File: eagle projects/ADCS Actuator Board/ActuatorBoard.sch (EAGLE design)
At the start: 231 parts, among them J11 TE_1-84953-1, J2 TE_1-84953-1, J4 TE_1-84953-1, J5 TE-1734829-3, U10 LM2917MX/NOPB, U11 BD6210F-E2, U12 TSV991AILT, U13 LM2917MX/NOPB, U14 ADS7841E_2K5, U16 DRV10970_MOTOR_DRIVERDRV10970, U17 LM2917MX/NOPB, U18 BD6210F-E2, U19 TSV991AILT, U20 ADS7841E_2K5, U5 BD6210F-E2, U6 DRV10970_MOTOR_DRIVERDRV10970, U7 DRV10970_MOTOR_DRIVERDRV10970, U8 TSV991AILT, U9 ADS7841E_2K5

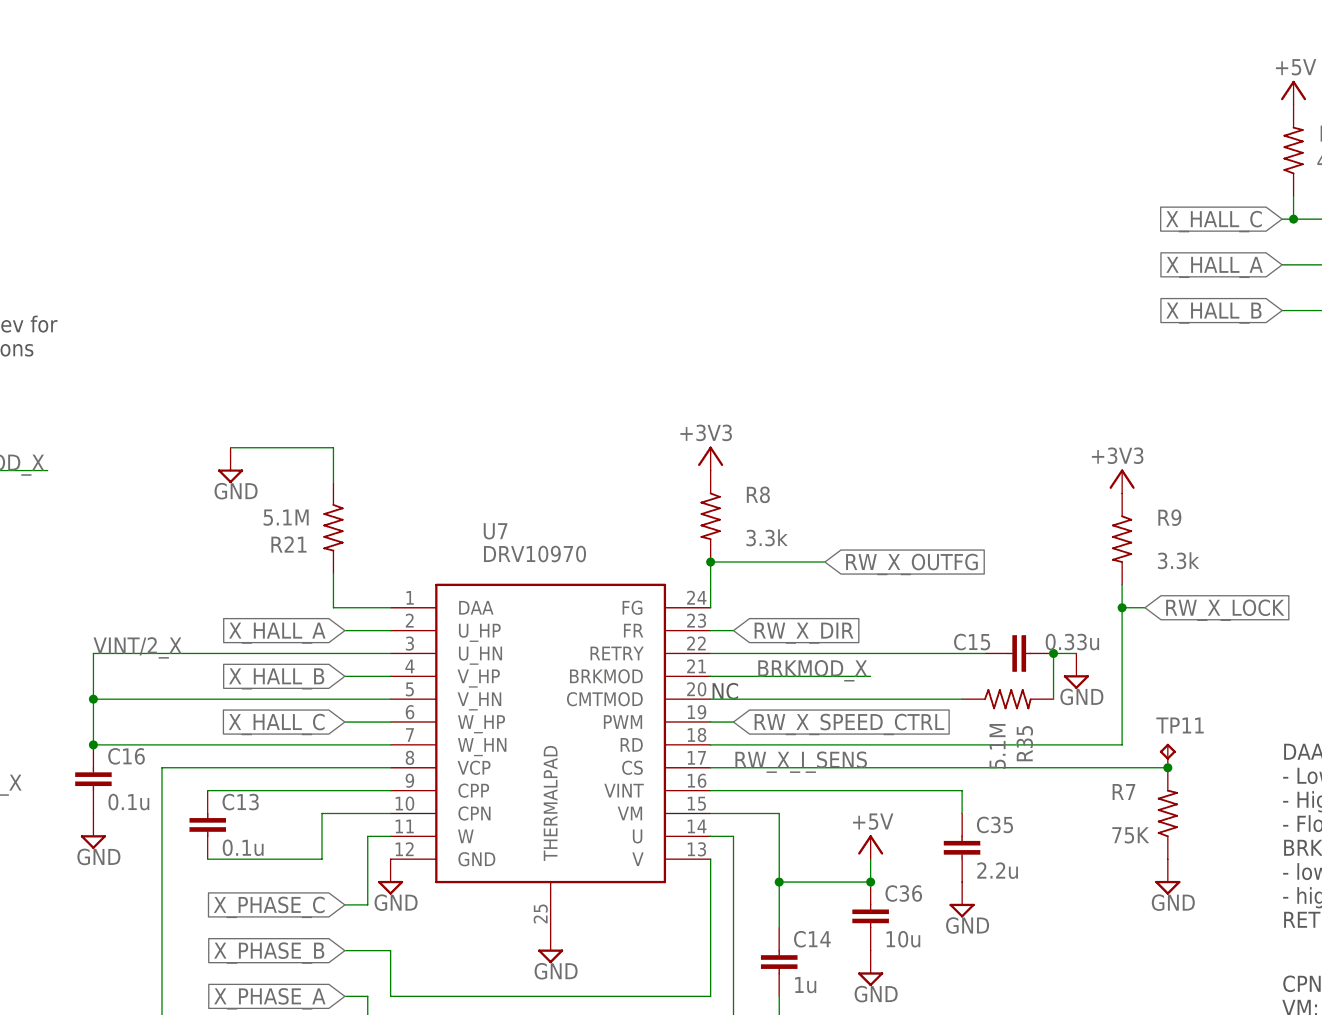
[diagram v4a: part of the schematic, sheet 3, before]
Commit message: Stitching vias, new current limit res for motors, updated motor retry cap
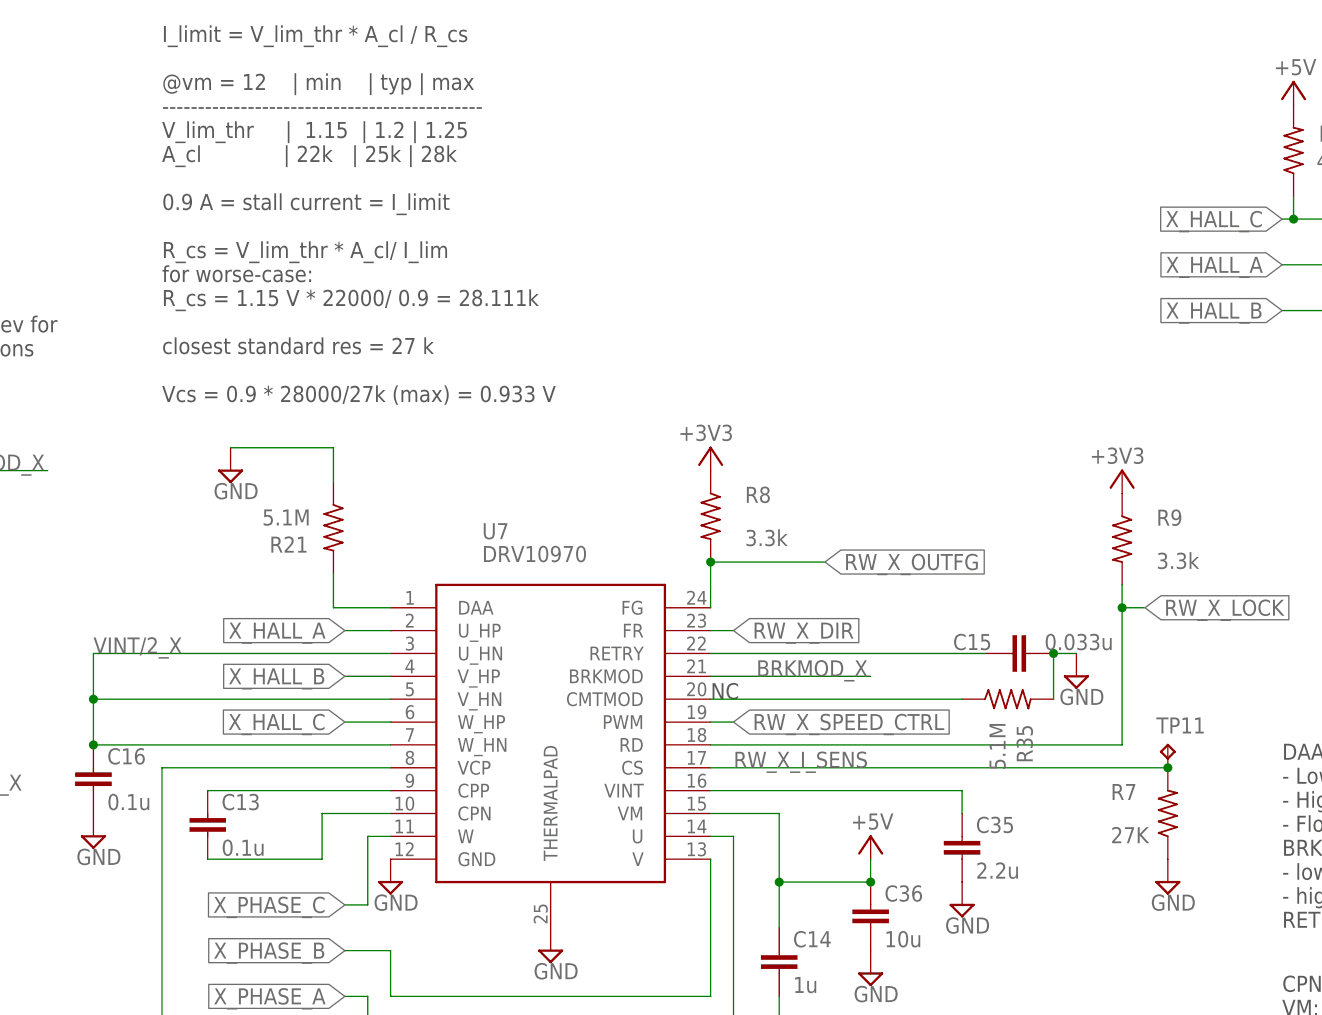
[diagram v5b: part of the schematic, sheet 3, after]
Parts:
- C15, C19, C57: value 0.33u -> 0.033u
- R104, R61, R7: value 75K -> 27K
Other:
- note added: "I_limit = V_lim_thr * A_cl / R_cs @vm = 12 | min | typ | max --------------------------------------------- V_lim_thr | 1.15 | 1.2 | 1.25 A_cl | 22k | 25k | 28k 0.9 A = stall current = I_limit R_cs = V_lim_thr * A_cl/ I_lim for worse-case: R_cs = 1.15 V * 22000/ 0.9 = 28.111k closest standard res = 27 k Vcs = 0.9 * 28000/27k (max) = 0.933 V"
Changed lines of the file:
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@@
 <schematic_group name="POWER54"/>
 <schematic_group name="TUNING-RES"/>
+<schematic_group name="I_LIM-CALC"/>
 </groups>
 <parts>
@@
 <part name="SUPPLY66" library="supply2" library_urn="urn:adsk.eagle:library:372" deviceset="GND" device=""/>
 <part name="SUPPLY67" library="supply2" library_urn="urn:adsk.eagle:library:372" deviceset="GND" device=""/>
-<part name="R61" library="rcl" library_urn="urn:adsk.eagle:library:334" deviceset="R-US_" device="R0603" package3d_urn="urn:adsk.eagle:package:23555/3" value="75K"/>
+<part name="R61" library="rcl" library_urn="urn:adsk.eagle:library:334" deviceset="R-US_" device="R0603" package3d_urn="urn:adsk.eagle:package:23555/3" value="27K"/>
 <part name="SUPPLY68" library="supply2" library_urn="urn:adsk.eagle:library:372" deviceset="GND" device=""/>
 <part name="P+28" library="supply1" library_urn="urn:adsk.eagle:library:371" deviceset="+5V" device=""/>
@@
 <part name="+3V15" library="supply1" library_urn="urn:adsk.eagle:library:371" deviceset="+3V3" device=""/>
 <part name="R62" library="rcl" library_urn="urn:adsk.eagle:library:334" deviceset="R-US_" device="R0603" package3d_urn="urn:adsk.eagle:package:23555/3" value="3.3k"/>
-<part name="C19" library="rcl" library_urn="urn:adsk.eagle:library:334" deviceset="C-EU" device="C0603" package3d_urn="urn:adsk.eagle:package:23616/2" value="0.33u"/>
+<part name="C19" library="rcl" library_urn="urn:adsk.eagle:library:334" deviceset="C-EU" device="C0603" package3d_urn="urn:adsk.eagle:package:23616/2" value="0.033u"/>
 <part name="SUPPLY70" library="supply2" library_urn="urn:adsk.eagle:library:372" deviceset="GND" device=""/>
 <part name="+3V16" library="supply1" library_urn="urn:adsk.eagle:library:371" deviceset="+3V3" device=""/>
@@
 <part name="SUPPLY1" library="supply2" library_urn="urn:adsk.eagle:library:372" deviceset="GND" device=""/>
 <part name="SUPPLY2" library="supply2" library_urn="urn:adsk.eagle:library:372" deviceset="GND" device=""/>
-<part name="R7" library="rcl" library_urn="urn:adsk.eagle:library:334" deviceset="R-US_" device="R0603" package3d_urn="urn:adsk.eagle:package:23555/3" value="75K"/>
+<part name="R7" library="rcl" library_urn="urn:adsk.eagle:library:334" deviceset="R-US_" device="R0603" package3d_urn="urn:adsk.eagle:package:23555/3" value="27K"/>
 <part name="SUPPLY6" library="supply2" library_urn="urn:adsk.eagle:library:372" deviceset="GND" device=""/>
 <part name="P+3" library="supply1" library_urn="urn:adsk.eagle:library:371" deviceset="+5V" device=""/>
@@
 <part name="+3V10" library="supply1" library_urn="urn:adsk.eagle:library:371" deviceset="+3V3" device=""/>
 <part name="R8" library="rcl" library_urn="urn:adsk.eagle:library:334" deviceset="R-US_" device="R0603" package3d_urn="urn:adsk.eagle:package:23555/3" value="3.3k"/>
-<part name="C15" library="rcl" library_urn="urn:adsk.eagle:library:334" deviceset="C-EU" device="C0603" package3d_urn="urn:adsk.eagle:package:23616/2" value="0.33u"/>
+<part name="C15" library="rcl" library_urn="urn:adsk.eagle:library:334" deviceset="C-EU" device="C0603" package3d_urn="urn:adsk.eagle:package:23616/2" value="0.033u"/>
 <part name="SUPPLY8" library="supply2" library_urn="urn:adsk.eagle:library:372" deviceset="GND" device=""/>
 <part name="+3V11" library="supply1" library_urn="urn:adsk.eagle:library:371" deviceset="+3V3" device=""/>
@@
 <part name="SUPPLY105" library="supply2" library_urn="urn:adsk.eagle:library:372" deviceset="GND" device=""/>
 <part name="SUPPLY106" library="supply2" library_urn="urn:adsk.eagle:library:372" deviceset="GND" device=""/>
-<part name="R104" library="rcl" library_urn="urn:adsk.eagle:library:334" deviceset="R-US_" device="R0603" package3d_urn="urn:adsk.eagle:package:23555/3" value="75K"/>
+<part name="R104" library="rcl" library_urn="urn:adsk.eagle:library:334" deviceset="R-US_" device="R0603" package3d_urn="urn:adsk.eagle:package:23555/3" value="27K"/>
 <part name="SUPPLY107" library="supply2" library_urn="urn:adsk.eagle:library:372" deviceset="GND" device=""/>
 <part name="P+42" library="supply1" library_urn="urn:adsk.eagle:library:371" deviceset="+5V" device=""/>
@@
 <part name="+3V25" library="supply1" library_urn="urn:adsk.eagle:library:371" deviceset="+3V3" device=""/>
 <part name="R105" library="rcl" library_urn="urn:adsk.eagle:library:334" deviceset="R-US_" device="R0603" package3d_urn="urn:adsk.eagle:package:23555/3" value="3.3k"/>
-<part name="C57" library="rcl" library_urn="urn:adsk.eagle:library:334" deviceset="C-EU" device="C0603" package3d_urn="urn:adsk.eagle:package:23616/2" value="0.33u"/>
+<part name="C57" library="rcl" library_urn="urn:adsk.eagle:library:334" deviceset="C-EU" device="C0603" package3d_urn="urn:adsk.eagle:package:23616/2" value="0.033u"/>
 <part name="SUPPLY109" library="supply2" library_urn="urn:adsk.eagle:library:372" deviceset="GND" device=""/>
 <part name="+3V26" library="supply1" library_urn="urn:adsk.eagle:library:371" deviceset="+3V3" device=""/>
@@
 <text x="7.62" y="167.64" size="1.778" layer="97">3-Pin header Jumper on this Rev for
 testing both mode configurations</text>
+<text x="58.42" y="162.56" size="1.778" layer="97" grouprefs="I_LIM-CALC">I_limit = V_lim_thr * A_cl / R_cs
+@vm = 12    | min    | typ | max
+---------------------------------------------
+V_lim_thr     |  1.15  | 1.2 | 1.25
+A_cl             | 22k   | 25k | 28k
+0.9 A = stall current = I_limit
+R_cs = V_lim_thr * A_cl/ I_lim
+for worse-case:
+R_cs = 1.15 V * 22000/ 0.9 = 28.111k
+closest standard res = 27 k
+Vcs = 0.9 * 28000/27k (max) = 0.933 V</text>
 </plain>
 <instances>

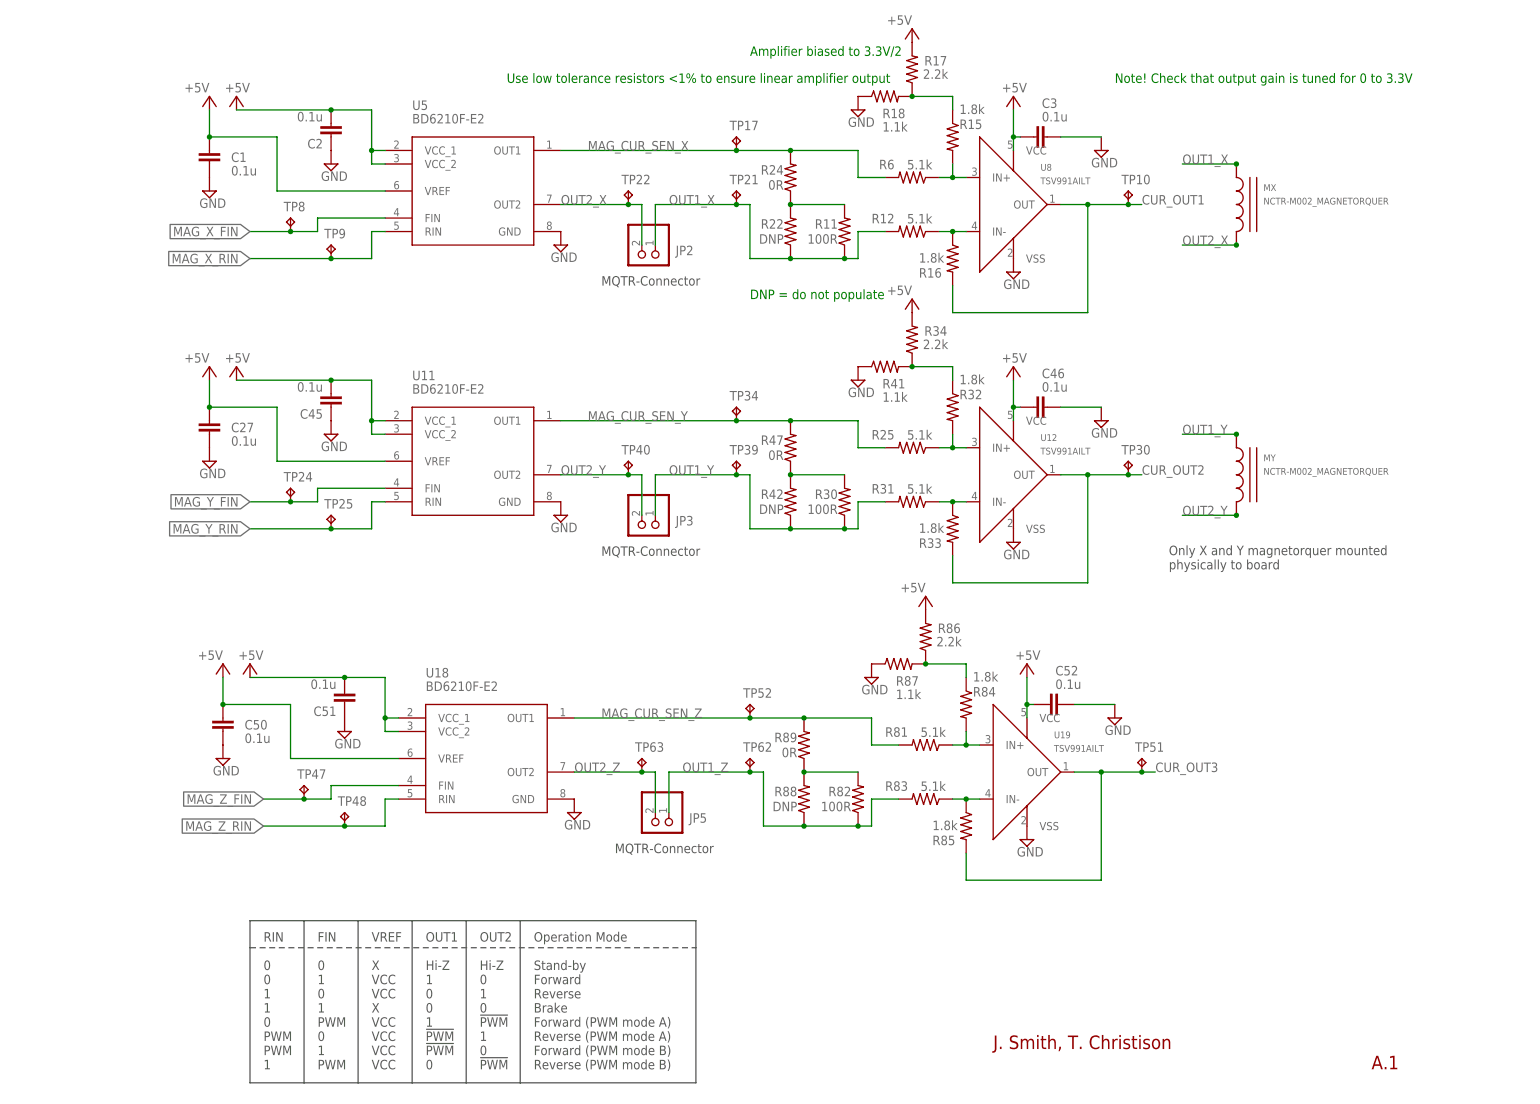
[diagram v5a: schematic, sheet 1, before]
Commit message: Replaced h-bridges with substitute part
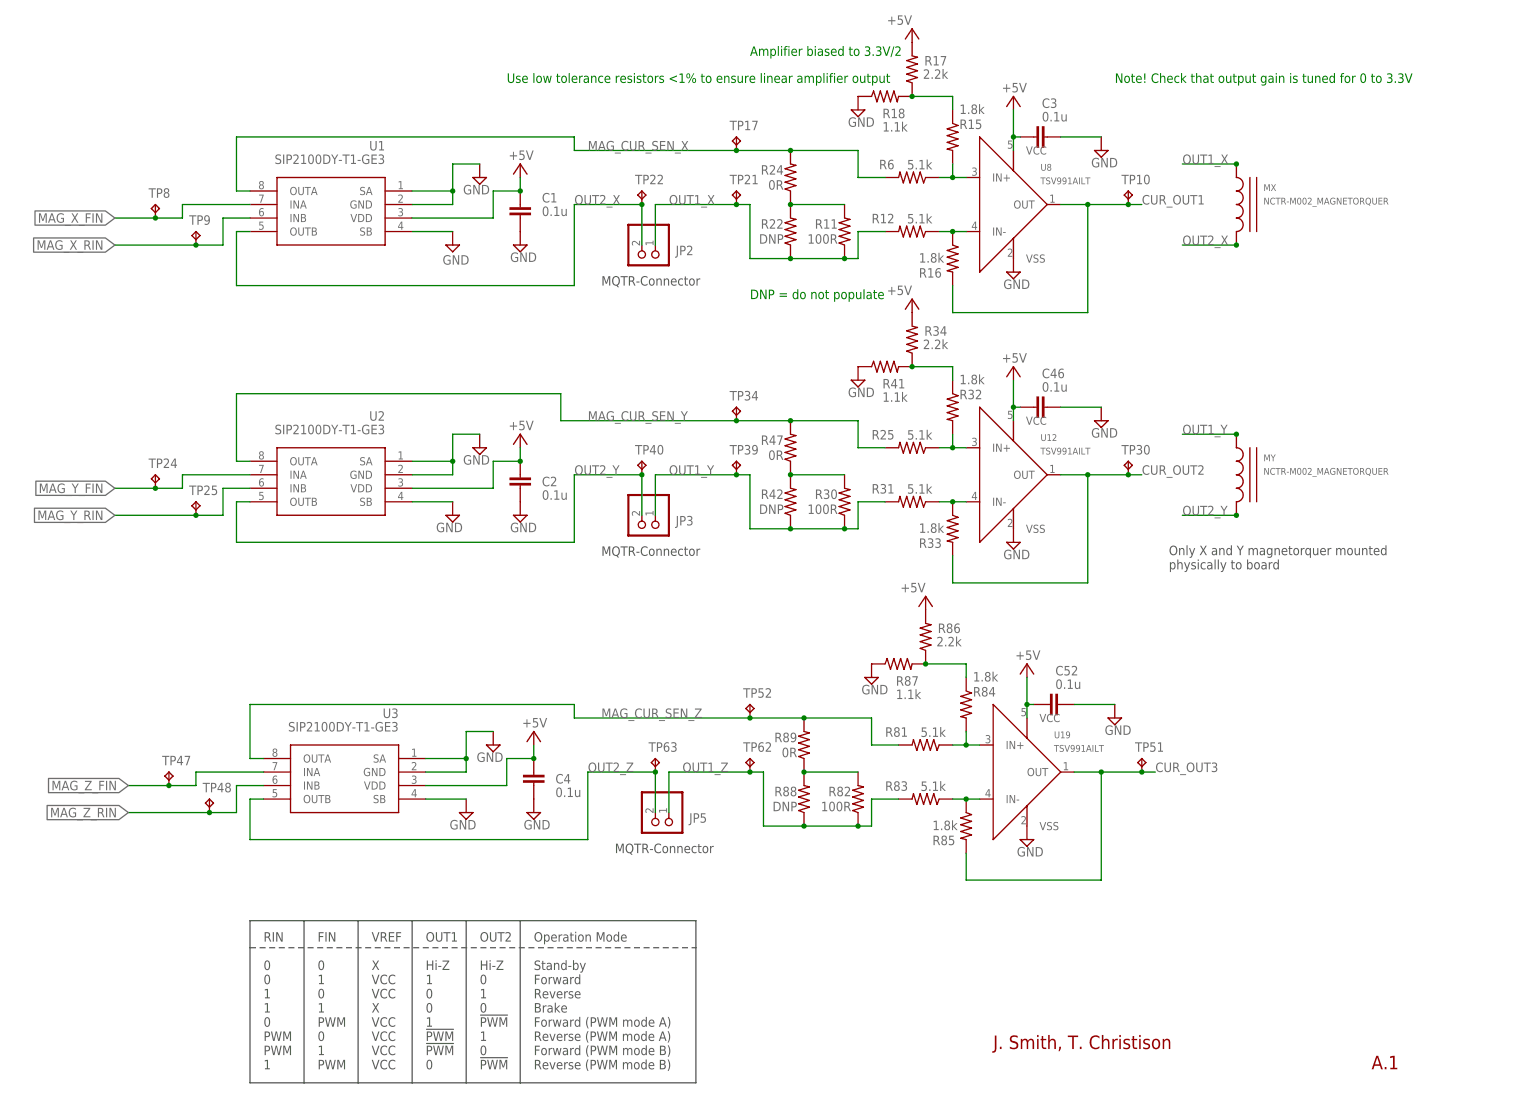
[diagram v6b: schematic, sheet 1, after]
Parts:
- removed C27, C45, C50, C51: 0.1u, rcl:C-EUC0603
- removed U11, U18, U5: BD6210F-E2, my_library:BD6210F-E2
- added C4: 0.1u, rcl:C-EUC0603
- added U1, U2, U3: SIP2100DY-T1-GE3, my_library:SIP2100DY-T1-GE3
- C31, C38, C61: value 0.01u -> 0.056u
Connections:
- net +5V: now also C4.2, U1.VDD, U2.VDD, U3.VDD; no longer C27.1, C45.2, C50.1, C51.2, U11.VCC_1, U11.VCC_2, U11.VREF, U18.VCC_1, U18.VCC_2, U18.VREF, U5.VCC_1, U5.VCC_2, U5.VREF
- net GND: now also C4.1, U1.GND, U1.SA, U1.SB, U2.GND, U2.SA, U2.SB, U3.GND, U3.SA, U3.SB; no longer C27.2, C45.1, C50.2, C51.1, U11.GND, U18.GND, U5.GND
- net MAG_CUR_SEN_X: now also U1.OUTA; no longer U5.OUT1
- net MAG_CUR_SEN_Y: now also U2.OUTA; no longer U11.OUT1
- net MAG_CUR_SEN_Z: now also U3.OUTA; no longer U18.OUT1
- net MAG_X_FIN: now also U1.INA; no longer U5.FIN
- net MAG_X_RIN: now also U1.INB; no longer U5.RIN
- net MAG_Y_FIN: now also U2.INA; no longer U11.FIN
- net MAG_Y_RIN: now also U2.INB; no longer U11.RIN
- net MAG_Z_FIN: now also U3.INA; no longer U18.FIN
- net MAG_Z_RIN: now also U3.INB; no longer U18.RIN
- net OUT2_X: now also U1.OUTB; no longer U5.OUT2
- net OUT2_Y: now also U2.OUTB; no longer U11.OUT2
- net OUT2_Z: now also U3.OUTB; no longer U18.OUT2
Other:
- moved on the sheet: C1, C2, TP22, TP24, TP25, TP40, TP47, TP48, TP63, TP8, TP9
